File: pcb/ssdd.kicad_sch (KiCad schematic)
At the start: 7 parts, among them U1 ATtiny861-20S

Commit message: remove unneeded caps and pullups
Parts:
- removed R1, R2: 10K, symbol Device:R

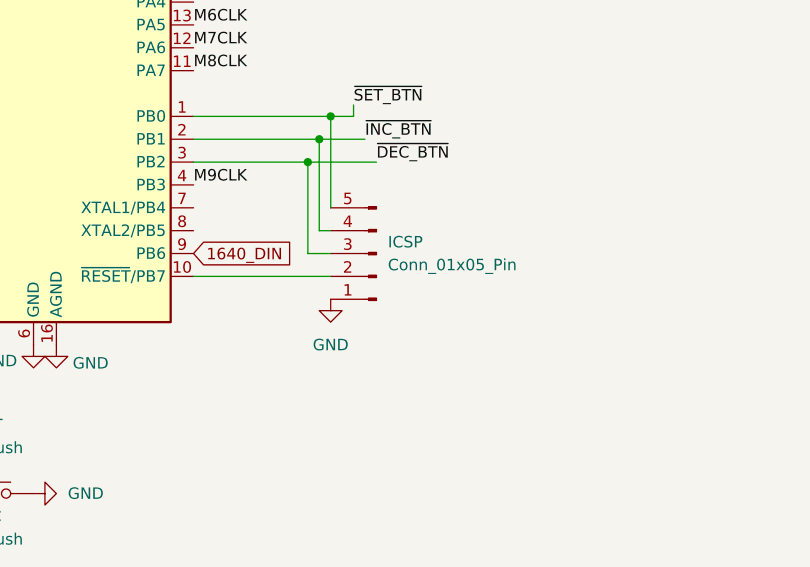
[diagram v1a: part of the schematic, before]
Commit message: expose vcc on icsp breakout
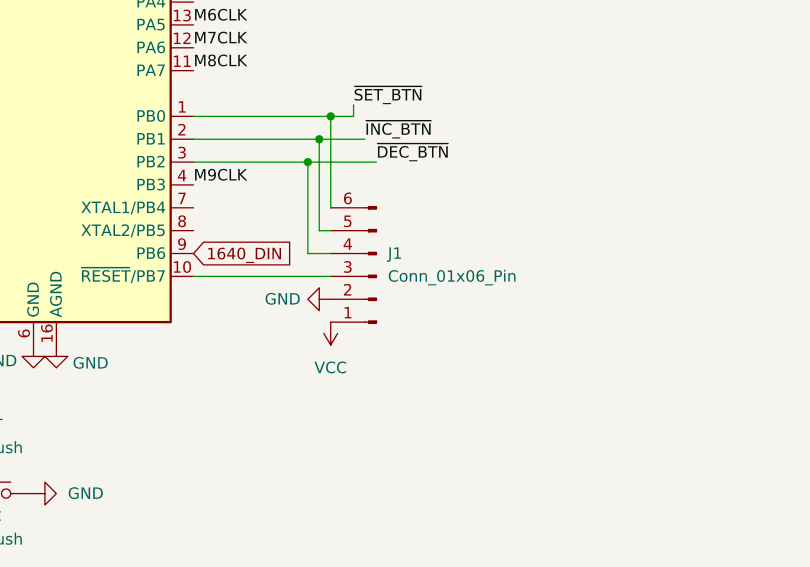
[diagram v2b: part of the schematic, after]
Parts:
- removed ICSP: Conn_01x05_Pin, symbol Connector:Conn_01x05_Pin
- added J1: Conn_01x06_Pin, symbol Connector:Conn_01x06_Pin
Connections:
- net GND: now also J1.2 (Pin_2)
- net ~{DEC_BTN}: now also J1.4 (Pin_4)
- net ~{INC_BTN}: now also J1.5 (Pin_5)
- net ~{SET_BTN}: now also J1.6 (Pin_6)
- net at U1.10 (~{RESET}/PB7): now also J1.3 (Pin_3)
- new net VCC: J1.1 (Pin_1)
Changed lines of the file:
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@@
 	)
 	(symbol
-		(lib_id "Connector:Conn_01x05_Pin")
-		(at 135.89 92.71 180)
+		(lib_id "Connector:Conn_01x06_Pin")
+		(at 135.89 95.25 180)
 		(unit 1)
 		(exclude_from_sim no)
@@
 		(dnp no)
 		(fields_autoplaced yes)
-		(property "Reference" "ICSP"
-			(at 137.16 91.4399 0)
+		(property "Reference" "J1"
+			(at 137.16 92.7099 0)
 			(effects
 				(font
@@
 			)
 		)
-		(property "Value" "Conn_01x05_Pin"
-			(at 137.16 93.9799 0)
+		(property "Value" "Conn_01x06_Pin"
+			(at 137.16 95.2499 0)
 			(effects
 				(font
@@
 		)
 		(property "Footprint" ""
-			(at 135.89 92.71 0)
+			(at 135.89 95.25 0)
 			(effects
 				(font
@@
 		)
 		(property "Datasheet" "~"
-			(at 135.89 92.71 0)
-			(effects
-				(font
-					(size 1.27 1.27)
-				)
-				(hide yes)
-			)
-		)
-		(property "Description" "Generic connector, single row, 01x05, script generated"
-			(at 135.89 92.71 0)
+			(at 135.89 95.25 0)
+			(effects
+				(font
+					(size 1.27 1.27)
+				)
+				(hide yes)
+			)
+		)
+		(property "Description" "Generic connector, single row, 01x06, script generated"
+			(at 135.89 95.25 0)
 			(effects
 				(font
@@
 		(pin "5"
 		)
-		(instances
-			(project ""
-				(path "/be5c4baa-09c6-44d9-9a7a-613f890eb055"
-					(reference "ICSP")
+		(pin "6"
+		)
+		(instances
+			(project ""
+				(path "/be5c4baa-09c6-44d9-9a7a-613f890eb055"
+					(reference "J1")
 					(unit 1)
 				)
@@
 				(path "/be5c4baa-09c6-44d9-9a7a-613f890eb055"
 					(reference "#PWR03")
+					(unit 1)
+				)
+			)
+		)
+	)
+	(symbol
+		(lib_id "power:VCC")
+		(at 130.81 100.33 180)
+		(unit 1)
+		(exclude_from_sim no)
+		(in_bom yes)
+		(on_board yes)
+		(dnp no)
+		(fields_autoplaced yes)
+		(property "Reference" "#PWR08"
+			(at 130.81 96.52 0)
+			(effects
+				(font
+					(size 1.27 1.27)
+				)
+				(hide yes)
+			)
+		)
+		(property "Value" "VCC"
+			(at 130.81 105.41 0)
+			(effects
+				(font
+					(size 1.27 1.27)
+				)
+			)
+		)
+		(property "Footprint" ""
+			(at 130.81 100.33 0)
+			(effects
+				(font
+					(size 1.27 1.27)
+				)
+				(hide yes)
+			)
+		)
+		(property "Datasheet" ""
+			(at 130.81 100.33 0)
+			(effects
+				(font
+					(size 1.27 1.27)
+				)
+				(hide yes)
+			)
+		)
+		(property "Description" "Power symbol creates a global label with name \"VCC\""
+			(at 130.81 100.33 0)
+			(effects
+				(font
+					(size 1.27 1.27)
+				)
+				(hide yes)
+			)
+		)
+		(pin "1"
+		)
+		(instances
+			(project ""
+				(path "/be5c4baa-09c6-44d9-9a7a-613f890eb055"
+					(reference "#PWR08")
 					(unit 1)
 				)
@@
 	(symbol
 		(lib_id "power:GND")
-		(at 130.81 97.79 0)
-		(unit 1)
-		(exclude_from_sim no)
-		(in_bom yes)
-		(on_board yes)
-		(dnp no)
-		(fields_autoplaced yes)
+		(at 130.81 97.79 270)
+		(unit 1)
+		(exclude_from_sim no)
+		(in_bom yes)
+		(on_board yes)
+		(dnp no)
 		(property "Reference" "#PWR09"
-			(at 130.81 104.14 0)
+			(at 124.46 97.79 0)
 			(effects
 				(font
@@
 		)
 		(property "Value" "GND"
-			(at 130.81 102.87 0)
-			(effects
-				(font
+			(at 125.476 97.79 90)
+			(effects
+				(font

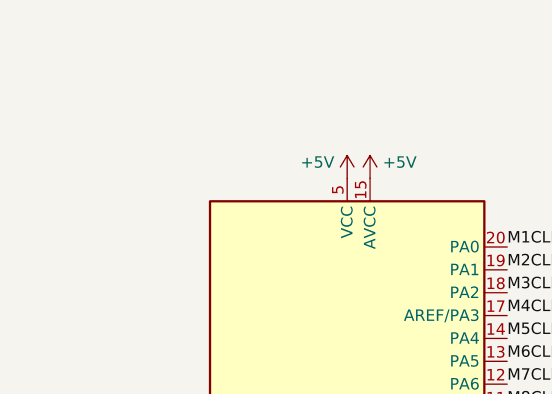
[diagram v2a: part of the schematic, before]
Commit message: add mcu caps
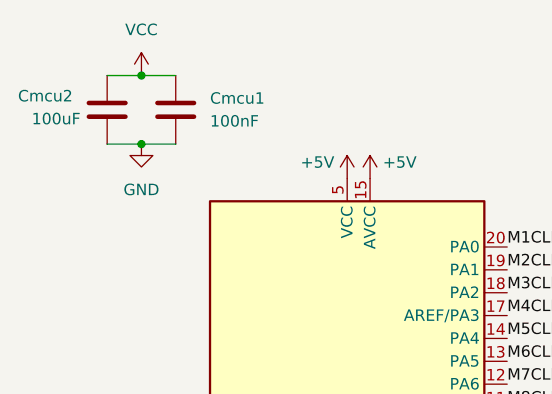
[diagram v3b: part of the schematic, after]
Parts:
- added Cmcu1: 100nF, symbol Device:C
- added Cmcu2: 100uF, symbol Device:C
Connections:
- net GND: now also Cmcu1.2, Cmcu2.2
- net VCC: now also Cmcu1.1, Cmcu2.1

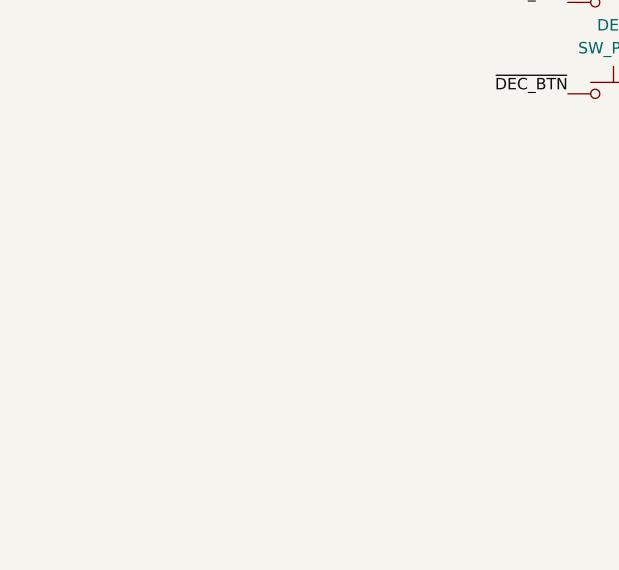
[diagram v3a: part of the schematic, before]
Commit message: USB-C power
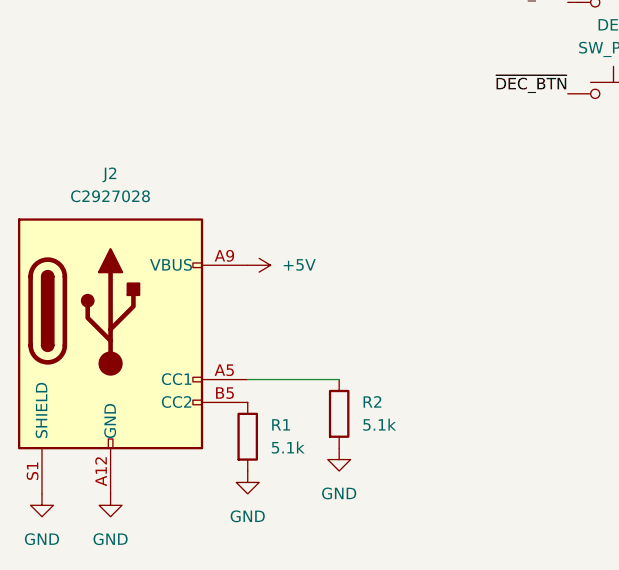
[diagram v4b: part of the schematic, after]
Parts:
- added J2: C2927028, symbol Connector:USB_C_Receptacle_PowerOnly_6P
- added R1, R2: 5.1k, symbol Device:R
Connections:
- net +5V: now also J2.A9 (VBUS), J2.B9 (VBUS)
- net GND: now also J2.A12 (GND), J2.B12 (GND), J2.S1 (SHIELD), R1.2, R2.2
- new net: J2.B5 (CC2), R1.1
- new net: J2.A5 (CC1), R2.1

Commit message: import C2927028 from jlcpcb
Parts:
- J2: footprint (none) -> ssdd:C2927028
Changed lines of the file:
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@@
 			)
 		)
-		(property "Footprint" ""
+		(property "Footprint" "ssdd:C2927028"
 			(at 40.64 163.83 0)
 			(effects

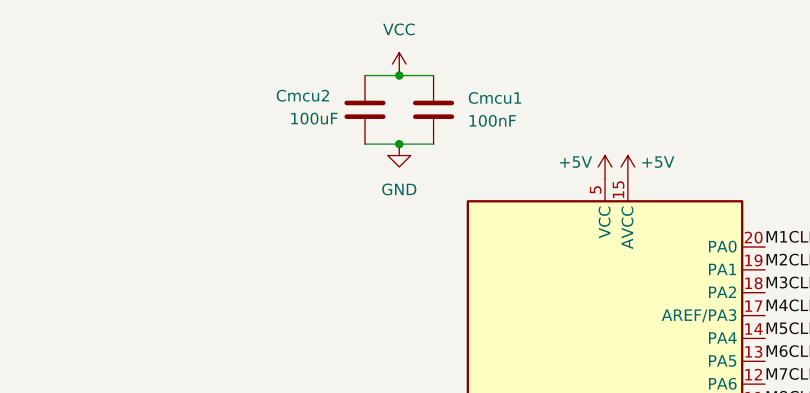
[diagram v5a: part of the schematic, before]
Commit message: 100nf decoupling caps
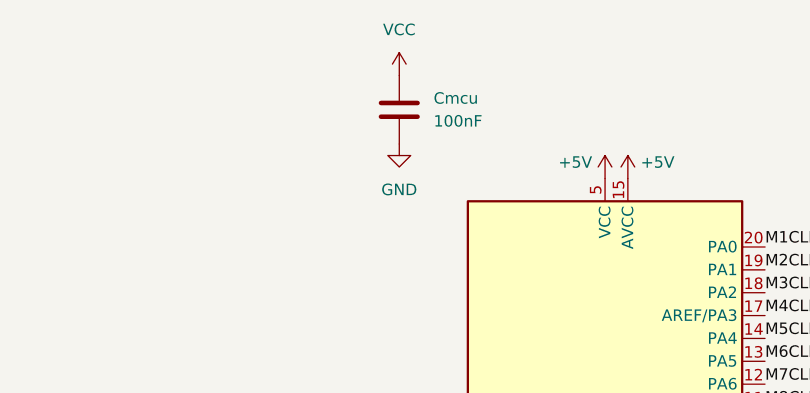
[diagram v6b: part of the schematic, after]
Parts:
- removed Cmcu2: 100uF, symbol Device:C
- renumbered Cmcu1 to Cmcu
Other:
- moved on the sheet: Cmcu
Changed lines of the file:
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@@
 	(paper "A4")
-	(junction
-		(at 74.93 35.56)
-		(diameter 0)
-		(color 0 0 0 0)
-	)
 	(junction
 		(at 128.27 82.55)
@@
 	)
 	(junction
-		(at 74.93 43.18)
-		(diameter 0)
-		(color 0 0 0 0)
-	)
-	(junction
 		(at 130.81 77.47)
 		(diameter 0)
@@
 	(wire
 		(pts
-			(xy 71.12 43.18) (xy 74.93 43.18)
+			(xy 52.07 171.45) (xy 62.23 171.45)
 		)
 		(stroke
@@
 	(wire
 		(pts
-			(xy 74.93 35.56) (xy 78.74 35.56)
+			(xy 129.54 80.01) (xy 134.62 80.01)
 		)
 		(stroke
@@
 	(wire
 		(pts
-			(xy 52.07 171.45) (xy 62.23 171.45)
+			(xy 115.57 80.01) (xy 129.54 80.01)
 		)
 		(stroke
@@
 	(wire
 		(pts
-			(xy 129.54 80.01) (xy 134.62 80.01)
-		)
-		(stroke
-			(width 0)
-			(type default)
-		)
-	)
-	(wire
-		(pts
-			(xy 71.12 35.56) (xy 74.93 35.56)
-		)
-		(stroke
-			(width 0)
-			(type default)
-		)
-	)
-	(wire
-		(pts
-			(xy 115.57 80.01) (xy 129.54 80.01)
-		)
-		(stroke
-			(width 0)
-			(type default)
-		)
-	)
-	(wire
-		(pts
 			(xy 130.81 87.63) (xy 130.81 77.47)
-		)
-		(stroke
-			(width 0)
-			(type default)
-		)
-	)
-	(wire
-		(pts
-			(xy 74.93 43.18) (xy 78.74 43.18)
 		)
 		(stroke
@@
 	)
 	(symbol
-		(lib_id "Device:C")
-		(at 71.12 39.37 0)
-		(unit 1)
-		(exclude_from_sim no)
-		(in_bom yes)
-		(on_board yes)
-		(dnp no)
-		(property "Reference" "Cmcu2"
-			(at 61.214 37.846 0)
-			(effects
-				(font
-					(size 1.27 1.27)
-				)
-				(justify left)
-			)
-		)
-		(property "Value" "100uF"
-			(at 62.738 40.386 0)
-			(effects
-				(font
-					(size 1.27 1.27)
-				)
-				(justify left)
-			)
-		)
-		(property "Footprint" ""
-			(at 72.0852 43.18 0)
-			(effects
-				(font
-					(size 1.27 1.27)
-				)
-				(hide yes)
-			)
-		)
-		(property "Datasheet" "~"
-			(at 71.12 39.37 0)
-			(effects
-				(font
-					(size 1.27 1.27)
-				)
-				(hide yes)
-			)
-		)
-		(property "Description" "Unpolarized capacitor"
-			(at 71.12 39.37 0)
-			(effects
-				(font
-					(size 1.27 1.27)
-				)
-				(hide yes)
-			)
-		)
-		(pin "1"
-		)
-		(pin "2"
-		)
-		(instances
-			(project ""
-				(path "/be5c4baa-09c6-44d9-9a7a-613f890eb055"
-					(reference "Cmcu2")
-					(unit 1)
-				)
-			)
-		)
-	)
-	(symbol
 		(lib_id "power:GND")
 		(at 97.79 139.7 90)
@@
 	(symbol
 		(lib_id "Device:C")
-		(at 78.74 39.37 0)
+		(at 74.93 39.37 0)
 		(unit 1)
 		(exclude_from_sim no)
@@
 		(dnp no)
 		(fields_autoplaced yes)
-		(property "Reference" "Cmcu1"
-			(at 82.55 38.0999 0)
+		(property "Reference" "Cmcu"
+			(at 78.74 38.0999 0)
 			(effects
 				(font
@@
 		)
 		(property "Value" "100nF"
-			(at 82.55 40.6399 0)
+			(at 78.74 40.6399 0)
 			(effects
 				(font
@@
 		)
 		(property "Footprint" ""
-			(at 79.7052 43.18 0)
+			(at 75.8952 43.18 0)
 			(effects
 				(font
@@
 		)
 		(property "Datasheet" "~"
-			(at 78.74 39.37 0)
+			(at 74.93 39.37 0)
 			(effects
 				(font
@@
 		)
 		(property "Description" "Unpolarized capacitor"
-			(at 78.74 39.37 0)
+			(at 74.93 39.37 0)
 			(effects
 				(font
@@
 			(project ""
 				(path "/be5c4baa-09c6-44d9-9a7a-613f890eb055"
-					(reference "Cmcu1")
-					(unit 1)
-				)
+					(reference "Cmcu")
+					(unit 1)
+				)
